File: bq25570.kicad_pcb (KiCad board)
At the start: 2 copper layers, 170.8 x 130.6 mm, 33 parts, among them J1 Conn_01x02_Male, J10 Conn_01x01_Male, J11 Conn_01x01_Male, J12 Conn_01x01_Male, J13 Conn_01x01_Male, J2 Conn_01x02_Male, J3 Conn_01x03_Male, J4 Conn_01x03_Male, J7 Conn_01x01_Male, J8 Conn_01x01_Male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

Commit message: PCB started
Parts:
- moved C5 69.9 mm to (123.4, 67.8), turned to 180 degrees
- moved R6 50.2 mm to (122.9, 76.7)
- moved D3 49.6 mm to (109.5, 90.4), turned to 180 degrees
- moved C3 49.5 mm to (115.3, 61.2)
- moved R10 48.7 mm to (104.9, 90.4), turned to 180 degrees
- moved C1 47.2 mm to (108.0, 71.1), turned to 270 degrees
- moved R7 46.6 mm to (122.9, 72.4), turned to 90 degrees
- moved C4 46.5 mm to (115.3, 64.8)
- moved R2 45.1 mm to (108.7, 81.0), turned to 270 degrees
- moved J8 42.4 mm to (121.2, 100.3)
- moved R4 42.1 mm to (118.9, 81.0), turned to 90 degrees
- moved R1 42.0 mm to (112.0, 81.0), turned to 90 degrees
- moved J1 40.5 mm to (89.9, 69.6), turned to 0 degrees
- moved C2 40.2 mm to (105.2, 81.0), turned to 270 degrees
- moved R9 39.3 mm to (104.9, 94.0), turned to 180 degrees
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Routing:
- net /GND: track 0.00 -> 67.7 mm
- net /VBAT: track 0.00 -> 24.5 mm
- net /OK_PROG: track 0.00 -> 12.0 mm
- net /VREF_SAMP: track 0.00 -> 12.0 mm
- net /OK_HYST: track 0.00 -> 11.2 mm
- net /VOUT_SET: track 0.00 -> 10.9 mm
- net /VSTOR: track 0.00 -> 8.73 mm
- net /VIN_DC: track 0.00 -> 5.33 mm
- net /VRDIV: track 0.00 -> 4.04 mm
- net /VBAT_OV: track 0.00 -> 3.36 mm
- net Net-(D3-Pad2): track 0.00 -> 2.52 mm
- net Net-(D2-Pad2): track 0.00 -> 2.52 mm
- net Net-(D1-Pad2): track 0.00 -> 2.52 mm
- net /LBUCK: track 0.00 -> 1.65 mm
- added copper zone on F.Cu, net /GND
- added copper zone on F.Cu, net /VIN_DC
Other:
- board size 170.8 x 130.6 mm -> 56.9 x 61 mm
- board text removed: "19/12/2019"
- board text removed: "BQ25570EVM"

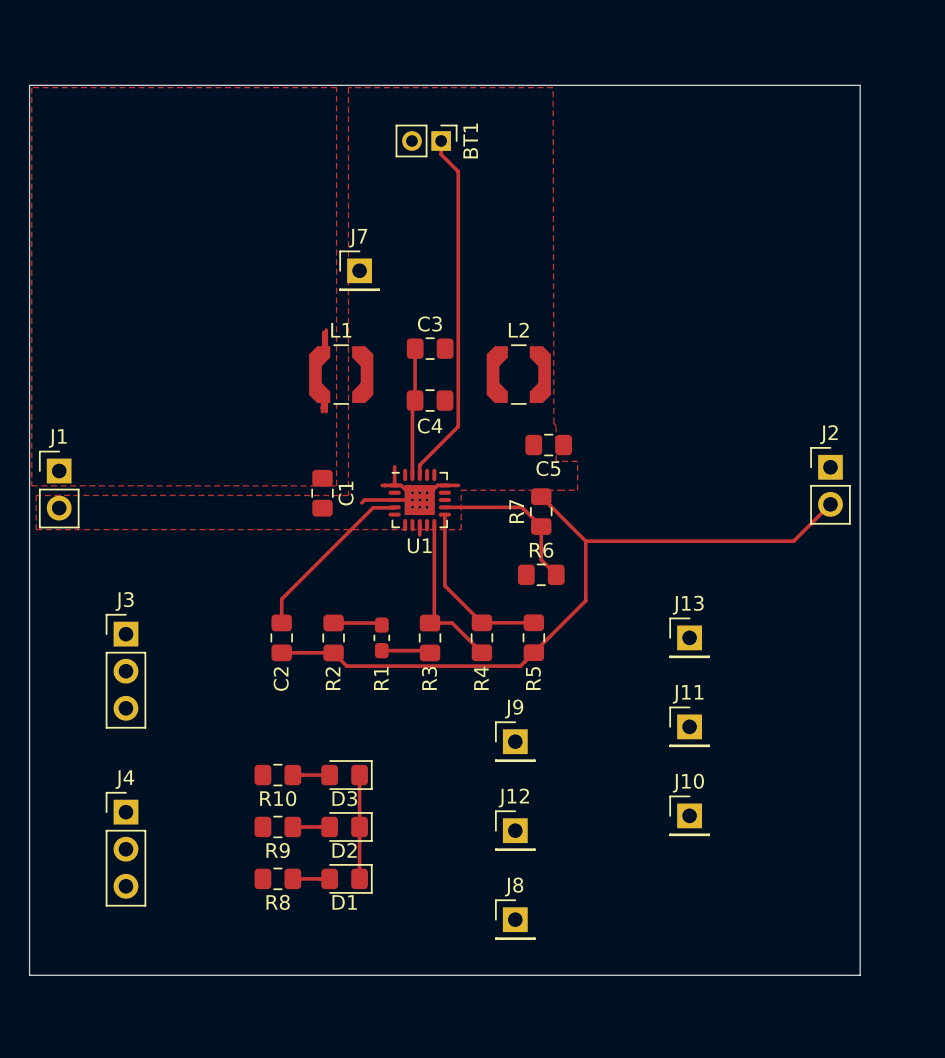
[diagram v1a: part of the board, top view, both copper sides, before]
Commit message: PCB layout done. Checking needed
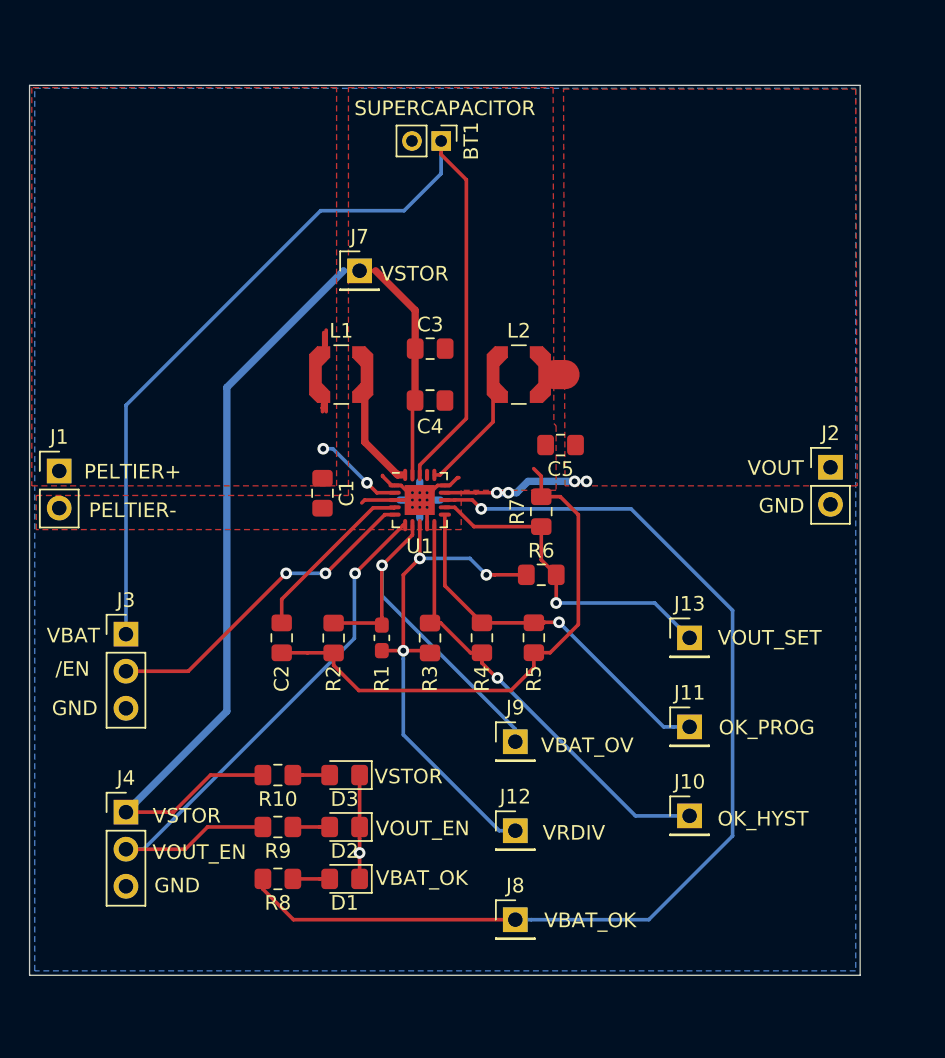
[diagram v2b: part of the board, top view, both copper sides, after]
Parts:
- moved C5 0.81 mm to (124.3, 67.8)
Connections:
- U1 pad 9: Net-(U1-Pad9) -> /GND
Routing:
- net /VBAT_OK: track 0.00 -> 74.4 mm, vias 0 -> 1
- net /VSTOR: track 8.73 -> 70.8 mm
- net /VBAT: track 24.5 -> 71.0 mm
- net /VOUT_EN: track 0.00 -> 40.9 mm, vias 0 -> 1
- net /VRDIV: track 4.04 -> 36.3 mm, vias 0 -> 3
- net /VBAT_OV: track 3.36 -> 26.9 mm, vias 0 -> 1
- net /EN: track 0.00 -> 22.8 mm, vias 0 -> 2
- net /OK_HYST: track 11.2 -> 30.5 mm, vias 0 -> 1
- net /VOUT: track 0.00 -> 17.9 mm, vias 0 -> 4
- net /OK_PROG: track 12.0 -> 25.7 mm, vias 0 -> 1
- net /VOUT_SET: track 10.9 -> 22.9 mm, vias 0 -> 1
- net /LBOOST: track 0.00 -> 11.6 mm
- net /LBUCK: track 1.65 -> 12.8 mm
- net /VIN_DC: track 5.33 -> 13.7 mm, vias 0 -> 2
- net /GND: track 67.7 -> 61.7 mm, vias 0 -> 1
- added copper zone on B.Cu, net /GND
- added copper zone on F.Cu, net /VOUT
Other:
- board text added: "/EN"
- board text added: "GND"
- board text added: "OK_HYST"
- board text added: "OK_PROG"
- board text added: "PELTIER+"
- board text added: "PELTIER-"
- board text added: "SUPERCAPACITOR"
- board text added: "VBAT"
- board text added: "VBAT_OK"
- board text added: "VBAT_OV"
- board text added: "VOUT"
- board text added: "VOUT_EN"
- board text added: "VOUT_SET"
- board text added: "VRDIV"
- board text added: "VSTOR"

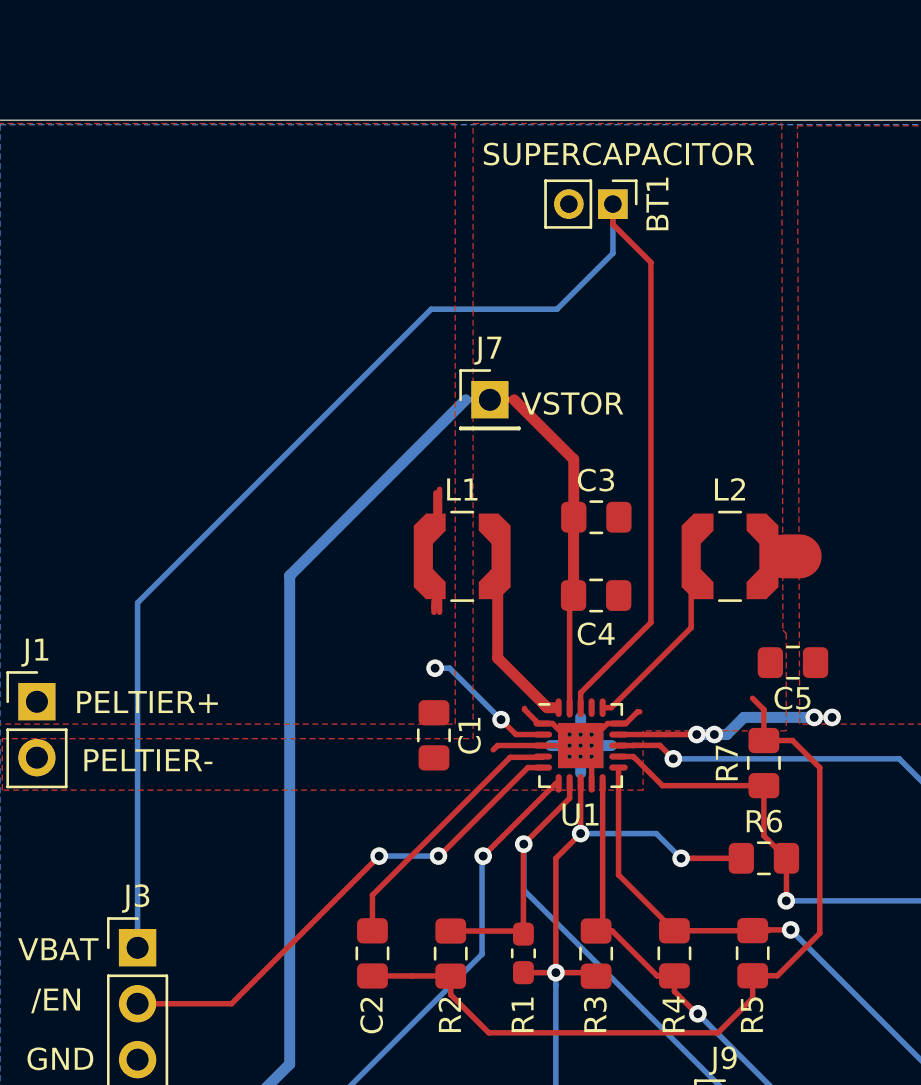
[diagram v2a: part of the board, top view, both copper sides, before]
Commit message: Footprint bt changed
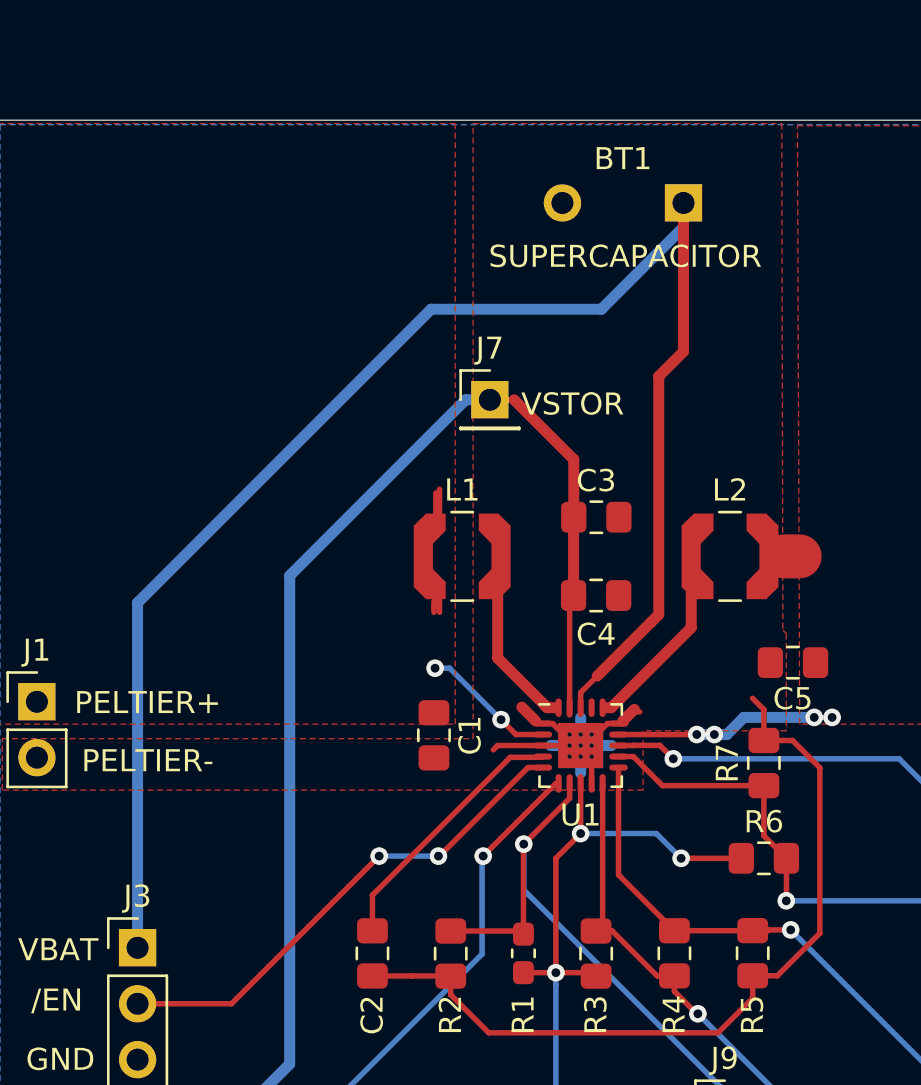
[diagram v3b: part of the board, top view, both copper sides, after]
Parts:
- BT1: footprint Connector_PinHeader_2.00mm:PinHeader_1x02_P2.00mm_Vertical -> Components:PinHeader_1x02_P5.50mm_Vertical
- moved BT1 0.46 mm to (116.5, 46.9), turned to 180 degrees
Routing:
- net /VBAT: track 71.0 -> 73.5 mm
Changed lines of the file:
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@@
     (thickness 1.6)
     (drawings 27)
-    (tracks 255)
+    (tracks 258)
     (zones 0)
     (modules 33)
@@
     )
   )
-  (module Connector_PinHeader_2.00mm:PinHeader_1x02_P2.00mm_Vertical (layer F.Cu)
-    (at 116.078 46.99 270)
-    (descr "Through hole straight pin header, 1x02, 2.00mm pitch, single row")
-    (tags "Through hole pin header THT 1x02 2.00mm single row")
-    (fp_text reference BT1 (at 0 -2.06 90) (layer F.SilkS)
-      (effects (font (size 1 1) (thickness 0.15)))
-    )
-    (fp_text value 5F (at 0 4.06 90) (layer F.Fab)
-      (effects (font (size 1 1) (thickness 0.15)))
-    )
-    (fp_text user %R (at 0 1) (layer F.Fab)
-      (effects (font (size 1 1) (thickness 0.15)))
-    )
-    (fp_line (start 1.5 -1.5) (end -1.5 -1.5) (layer F.CrtYd) (width 0.05))
-    (fp_line (start 1.5 3.5) (end 1.5 -1.5) (layer F.CrtYd) (width 0.05))
-    (fp_line (start -1.5 3.5) (end 1.5 3.5) (layer F.CrtYd) (width 0.05))
-    (fp_line (start -1.5 -1.5) (end -1.5 3.5) (layer F.CrtYd) (width 0.05))
-    (fp_line (start -1.06 -1.06) (end 0 -1.06) (layer F.SilkS) (width 0.12))
-    (fp_line (start -1.06 0) (end -1.06 -1.06) (layer F.SilkS) (width 0.12))
-    (fp_line (start -1.06 1) (end 1.06 1) (layer F.SilkS) (width 0.12))
-    (fp_line (start 1.06 1) (end 1.06 3.06) (layer F.SilkS) (width 0.12))
-    (fp_line (start -1.06 1) (end -1.06 3.06) (layer F.SilkS) (width 0.12))
-    (fp_line (start -1.06 3.06) (end 1.06 3.06) (layer F.SilkS) (width 0.12))
-    (fp_line (start -1 -0.5) (end -0.5 -1) (layer F.Fab) (width 0.1))
-    (fp_line (start -1 3) (end -1 -0.5) (layer F.Fab) (width 0.1))
-    (fp_line (start 1 3) (end -1 3) (layer F.Fab) (width 0.1))
-    (fp_line (start 1 -1) (end 1 3) (layer F.Fab) (width 0.1))
-    (fp_line (start -0.5 -1) (end 1 -1) (layer F.Fab) (width 0.1))
-    (pad 2 thru_hole oval (at 0 2 270) (size 1.35 1.35) (drill 0.8) (layers *.Cu *.Mask)
-      (net 1 /GND))
-    (pad 1 thru_hole rect (at 0 0 270) (size 1.35 1.35) (drill 0.8) (layers *.Cu *.Mask)
+  (module Components:PinHeader_1x02_P5.50mm_Vertical (layer F.Cu)
+    (at 116.5352 46.9392 180)
+    (fp_text reference BT1 (at 0 2) (layer F.SilkS)
+      (effects (font (size 1 1) (thickness 0.15)))
+    )
+    (fp_text value 5F (at 0 -2) (layer F.Fab)
+      (effects (font (size 1 1) (thickness 0.15)))
+    )
+    (pad 1 thru_hole rect (at -2.75 0 180) (size 1.7 1.7) (drill 1) (layers *.Cu *.Mask)
       (net 2 /VBAT))
-    (model ${KISYS3DMOD}/Connector_PinHeader_2.00mm.3dshapes/PinHeader_1x02_P2.00mm_Vertical.wrl
-      (at (xyz 0 0 0))
-      (scale (xyz 1 1 1))
-      (rotate (xyz 0 0 0))
-    )
+    (pad 2 thru_hole circle (at 2.75 0 180) (size 1.7 1.7) (drill 1) (layers *.Cu *.Mask)
+      (net 1 /GND))
   )
   (gr_text OK_HYST (at 138.1252 93.4212) (layer F.SilkS)
@@
     (effects (font (size 1 1) (thickness 0.15)))
   )
-  (gr_text SUPERCAPACITOR (at 116.332 44.7548) (layer F.SilkS)
+  (gr_text SUPERCAPACITOR (at 116.6368 49.3776) (layer F.SilkS)
     (effects (font (size 1 1) (thickness 0.15)))
   )
@@
   (segment (start 112.0648 69.9516) (end 112.0648 69.9008) (width 0.25) (layer F.Cu) (net 1))
   (segment (start 112.89242 70.58482) (end 112.69802 70.58482) (width 0.25) (layer F.Cu) (net 1))
-  (segment (start 112.69802 70.58482) (end 112.0648 69.9516) (width 0.25) (layer F.Cu) (net 1))
+  (segment (start 112.5728 70.4723) (end 111.93958 69.83908) (width 0.5) (layer F.Cu) (net 1))
   (segment (start 117.1956 70.0532) (end 117.2972 70.0532) (width 0.25) (layer F.Cu) (net 1))
   (segment (start 116.33242 70.58482) (end 116.66398 70.58482) (width 0.25) (layer F.Cu) (net 1))
-  (segment (start 116.66398 70.58482) (end 117.1956 70.0532) (width 0.25) (layer F.Cu) (net 1))
+  (segment (start 116.5225 70.4723) (end 117.05412 69.94068) (width 0.5) (layer F.Cu) (net 1))
   (segment (start 114.61242 71.58482) (end 114.61242 72.83958) (width 0.5) (layer B.Cu) (net 1))
   (segment (start 116.01958 71.58482) (end 114.61242 71.58482) (width 0.5) (layer B.Cu) (net 1))
@@
   (segment (start 108.712 82.06) (end 108.712 82.9056) (width 0.25) (layer F.Cu) (net 1))
   (segment (start 108.712 82.9056) (end 110.4392 84.6328) (width 0.25) (layer F.Cu) (net 1))
-  (segment (start 116.078 49.2252) (end 116.078 46.99) (width 0.25) (layer B.Cu) (net 2))
-  (segment (start 113.538 51.7652) (end 116.078 49.2252) (width 0.25) (layer B.Cu) (net 2))
-  (segment (start 107.822798 51.7652) (end 113.538 51.7652) (width 0.25) (layer B.Cu) (net 2))
-  (segment (start 94.488 80.772) (end 94.488 65.099998) (width 0.25) (layer B.Cu) (net 2))
-  (segment (start 94.488 65.099998) (end 107.822798 51.7652) (width 0.25) (layer B.Cu) (net 2))
-  (segment (start 114.61242 69.18982) (end 114.61242 69.86482) (width 0.25) (layer F.Cu) (net 2))
-  (segment (start 117.8052 65.99704) (end 114.61242 69.18982) (width 0.25) (layer F.Cu) (net 2))
-  (segment (start 117.8052 49.6422) (end 117.8052 65.99704) (width 0.25) (layer F.Cu) (net 2))
-  (segment (start 116.078 46.99) (end 116.078 47.915) (width 0.25) (layer F.Cu) (net 2))
-  (segment (start 116.078 47.915) (end 117.8052 49.6422) (width 0.25) (layer F.Cu) (net 2))
+  (segment (start 119.2852 48.0392) (end 119.2852 46.9392) (width 0.5) (layer B.Cu) (net 2))
+  (segment (start 115.5592 51.7652) (end 119.2852 48.0392) (width 0.5) (layer B.Cu) (net 2))
+  (segment (start 107.822798 51.7652) (end 115.5592 51.7652) (width 0.5) (layer B.Cu) (net 2))
+  (segment (start 94.488 65.099998) (end 107.822798 51.7652) (width 0.5) (layer B.Cu) (net 2))
+  (segment (start 94.488 80.772) (end 94.488 65.099998) (width 0.5) (layer B.Cu) (net 2))
+  (segment (start 117.8052 65.99704) (end 117.8052 65.9892) (width 0.25) (layer F.Cu) (net 2))
+  (segment (start 117.8052 65.9892) (end 118.1608 65.6336) (width 0.5) (layer F.Cu) (net 2))
+  (segment (start 118.1608 65.6336) (end 118.1608 54.8132) (width 0.5) (layer F.Cu) (net 2))
+  (segment (start 119.2852 53.6888) (end 119.2852 46.9392) (width 0.5) (layer F.Cu) (net 2))
+  (segment (start 118.1608 54.8132) (end 119.2852 53.6888) (width 0.5) (layer F.Cu) (net 2))
+  (segment (start 114.61242 69.86482) (end 114.61242 69.18198) (width 0.25) (layer F.Cu) (net 2))
+  (segment (start 117.8052 65.9892) (end 115.3668 68.4276) (width 0.5) (layer F.Cu) (net 2))
+  (segment (start 115.3668 68.4276) (end 114.61242 69.18198) (width 0.25) (layer F.Cu) (net 2))
   (segment (start 108.038 61.4345) (end 108.038 60.11) (width 0.25) (layer F.Cu) (net 3))
   (segment (start 108.038 61.4345) (end 108.038 61.126) (width 0.25) (layer F.Cu) (net 3))
@@
   (segment (start 101.3968 86.0552) (end 94.5212 92.9308) (width 0.5) (layer B.Cu) (net 5))
   (segment (start 101.3968 63.8732) (end 101.3968 86.0552) (width 0.5) (layer B.Cu) (net 5))
-  (segment (start 110.49 55.88) (end 109.39 55.88) (width 0.25) (layer B.Cu) (net 5))
+  (segment (start 110.49 55.88) (end 109.39 55.88) (width 0.5) (layer B.Cu) (net 5))
   (segment (start 109.39 55.88) (end 101.3968 63.8732) (width 0.5) (layer B.Cu) (net 5))
   (segment (start 97.7392 92.964) (end 94.488 92.964) (width 0.25) (layer F.Cu) (net 5))
@@
   (segment (start 113.4364 69.86482) (end 113.09562 69.86482) (width 0.5) (layer F.Cu) (net 18))
   (segment (start 119.634 64.637) (end 119.634 62.992) (width 0.25) (layer F.Cu) (net 19))
-  (segment (start 119.634 66.23324) (end 119.634 64.637) (width 0.25) (layer F.Cu) (net 19))
-  (segment (start 116.00242 69.86482) (end 119.634 66.23324) (width 0.25) (layer F.Cu) (net 19))
-  (segment (start 115.61242 69.86482) (end 116.00242 69.86482) (width 0.25) (layer F.Cu) (net 19))
+  (segment (start 119.634 66.23324) (end 119.634 64.637) (width 0.5) (layer F.Cu) (net 19))
+  (segment (start 116.00242 69.86482) (end 119.634 66.23324) (width 0.5) (layer F.Cu) (net 19))
   (segment (start 120.1395 61.499) (end 120.204 61.4345) (width 0.25) (layer F.Cu) (net 19))
   (segment (start 119.6555 61.499) (end 120.1395 61.499) (width 0.25) (layer F.Cu) (net 19))
@@
   (segment (start 120.18 61.4585) (end 120.204 61.4345) (width 0.25) (layer F.Cu) (net 19))
   (segment (start 120.18 61.9445) (end 120.18 61.4585) (width 0.25) (layer F.Cu) (net 19))
+  (segment (start 116.00242 69.86482) (end 115.78802 69.86482) (width 0.5) (layer F.Cu) (net 19))
   (zone (net 3) (net_name /VIN_DC) (layer F.Cu) (hatch edge 0.508)
     (connect_pads (clearance 0.508))

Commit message: Removing older files
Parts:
- C4: value 0.01μF -> 10nF
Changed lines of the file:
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@@
       (effects (font (size 1 1) (thickness 0.15)))
     )
-    (fp_text value 0.01μF (at 0 1.65) (layer F.Fab)
+    (fp_text value 10nF (at 0 1.65) (layer F.Fab)
       (effects (font (size 1 1) (thickness 0.15)))
     )
